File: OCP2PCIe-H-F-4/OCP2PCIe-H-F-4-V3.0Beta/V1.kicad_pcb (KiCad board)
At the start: 2 copper layers, 112.1 x 78.2 mm, 29 parts, among them J1 PCIe_x8, J2 Conn_02x40_Top_Bottom, J3 Conn_01x02, J4 Conn_01x02, U1 DM02, U2 9DBL411B

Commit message: fixed
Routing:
- net GND: track 160.2 -> 159.4 mm, vias 118 -> 123
- net (no net): vias 5 -> 0

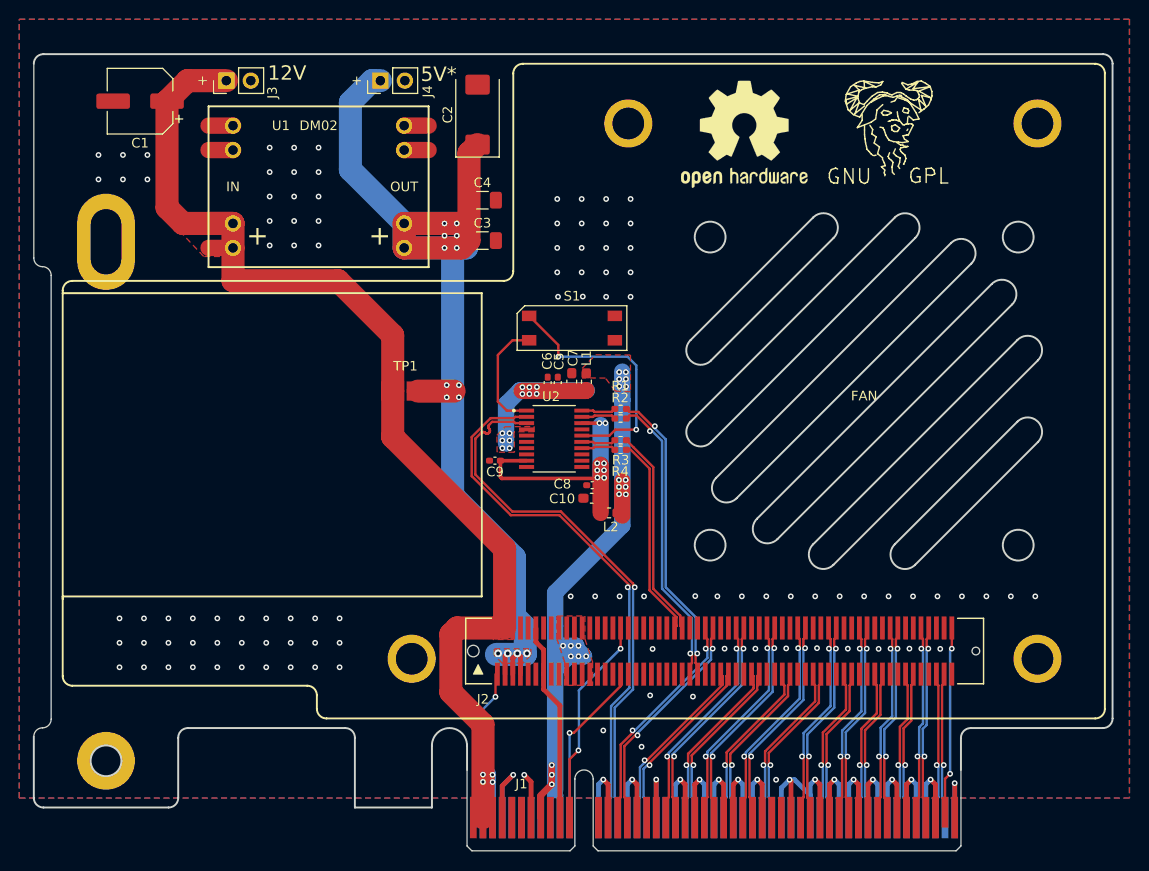
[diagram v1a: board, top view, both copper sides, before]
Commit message: tuning pcie lane
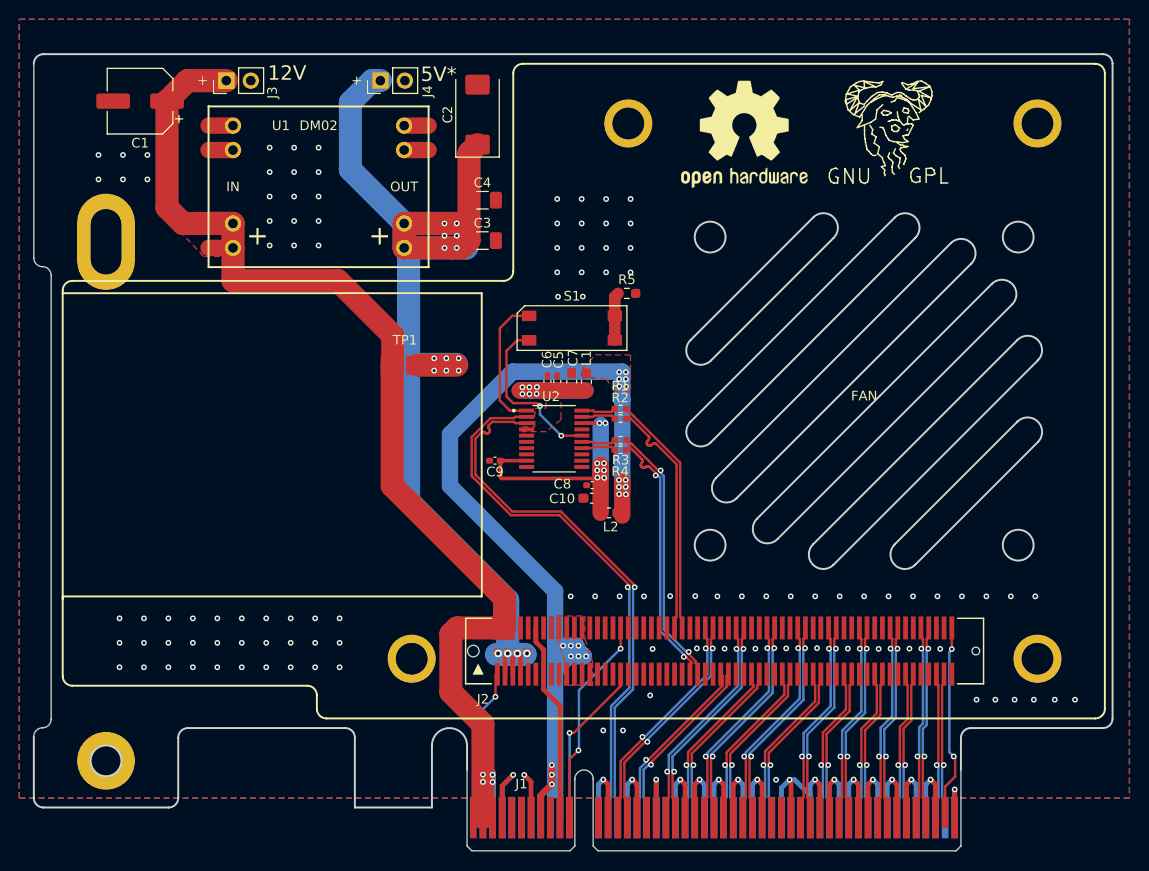
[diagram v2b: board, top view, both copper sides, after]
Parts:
- added R5: 100ohm, Resistor_SMD:R_0603_1608Metric_Pad0.98x0.95mm_HandSolder, F.Cu at (149.6, 76.1)
- R1: value R -> 34.46
- moved TP1 2.70 mm to (126.5, 83.5)
- moved C5 0.16 mm to (142.4, 85.2)
- moved C6 0.15 mm to (141.3, 85.2)
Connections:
- R1 pad 1: REFCLK1- -> REFCLK0-
- R1 pad 2: DIF1_N -> DIF0_N
- R2 pad 1: REFCLK1+ -> REFCLK0+
- R2 pad 2: DIF1_P -> DIF0_P
- R3 pad 1: REFCLK0- -> REFCLK1-
- R3 pad 2: DIF0_N -> DIF1_N
- R4 pad 1: REFCLK0+ -> REFCLK1+
- R4 pad 2: DIF0_P -> DIF1_P
- S1 pad 3: GND -> Net-(R5-Pad1)
- S1 pad 4: GND -> Net-(R5-Pad1)
- U2 pad 1: OE1 -> OE0
- U2 pad 14: DIF0_P -> DIF1_P
- U2 pad 15: DIF0_N -> DIF1_N
- U2 pad 16: OE0 -> OE1
- U2 pad 19: DIF1_P -> DIF0_P
- U2 pad 20: DIF1_N -> DIF0_N
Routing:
- net +3V3: track 72.1 -> 100.3 mm
- net OE0: track 26.6 -> 14.3 mm, vias 2 -> 0
- net P5V_AUX: track 122.7 -> 129.3 mm, vias 14 -> 16
- net 3V3_A: track 19.8 -> 13.8 mm, vias 12 -> 6
- net OE1: track 12.1 -> 17.6 mm, vias 0 -> 2
- net Net-(R5-Pad1): track 0.00 -> 5.01 mm
- net REFCLK0+: track 21.0 -> 25.2 mm
- net REFCLK1-: track 31.4 -> 27.8 mm
- net REFCLK0-: track 21.9 -> 25.2 mm
- net REFCLK1+: track 30.8 -> 27.8 mm
- net HSI1_N: track 19.4 -> 18.1 mm
- net GND: track 159.4 -> 158.1 mm, vias 123 -> 128
- net HSI1_P: track 19.2 -> 18.1 mm
